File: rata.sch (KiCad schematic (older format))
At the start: 4 parts, among them J1 USB_B, J2 Soldering points, U1 ILC4-5_7L

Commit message: Add files via upload
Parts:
- added G1: LOGO, rata:stamp, symbol rata:LOGO
- added H1, H2, H3, H4: MountingHole, rata:hole_D3.5mm, symbol Mechanical:MountingHole
- F1: footprint (none) -> Fuse:Fuse_1206_3216Metric_Pad1.42x1.75mm_HandSolder
- J1: footprint (none) -> Connector_USB:USB_B_OST_USB-B1HSxx_Horizontal
- J2: footprint (none) -> Connector_Wire:SolderWire-0.5sqmm_1x02_P4.6mm_D0.9mm_OD2.1mm
- U1: footprint (none) -> rata:ILC4-5_7L

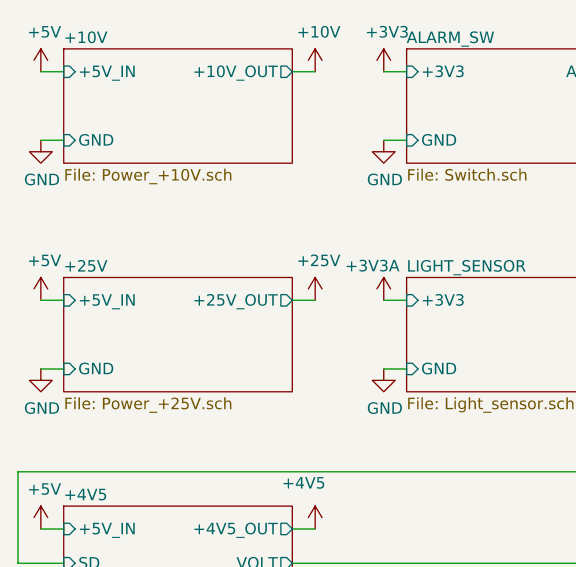
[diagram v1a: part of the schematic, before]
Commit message: Resistors values corrected to correspond actual values
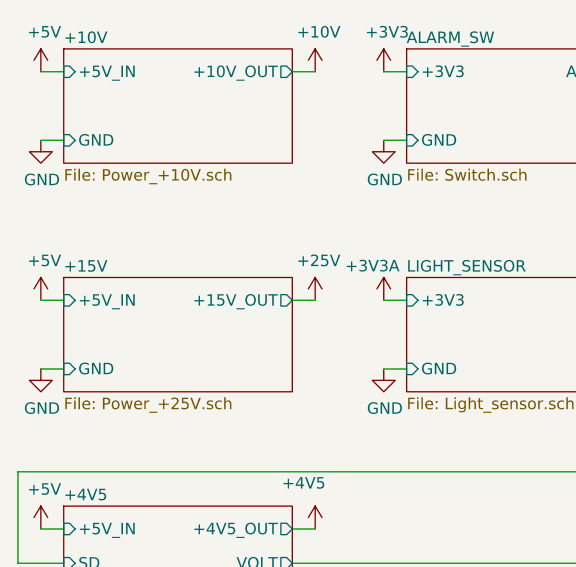
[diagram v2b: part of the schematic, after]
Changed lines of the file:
@@
-$EndSheet
-$Sheet
-S 1000 6000 1000 500
-U 60DF0860
-F0 "+25V" 50
-F1 "Power_+25V.sch" 50
-F2 "+5V_IN" I L 1000 6100 50
-F3 "+25V_OUT" O R 2000 6100 50
-F4 "GND" I L 1000 6400 50
 $EndSheet
 $Sheet
@@
 Wire Bus Line
 	8350 1300 10000 1300
+$Sheet
+S 1000 6000 1000 500
+U 60DF0860
+F0 "+15V" 50
+F1 "Power_+25V.sch" 50
+F2 "+5V_IN" I L 1000 6100 50
+F3 "GND" I L 1000 6400 50
+F4 "+15V_OUT" O R 2000 6100 50
+$EndSheet
 $EndSCHEMATC
